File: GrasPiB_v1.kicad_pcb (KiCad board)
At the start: 2 copper layers, 85 x 56 mm, 45 parts, among them J1 DB9_Male, J2 Conn_GPIB, J3 JST_PH, J4 JST_PH, J5 3,5mm Pitch, J6 10pin IDC, U1 RPi_GPIO, U2 MAX3232, U3 SN75160BDW, U4 SN75161BDW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

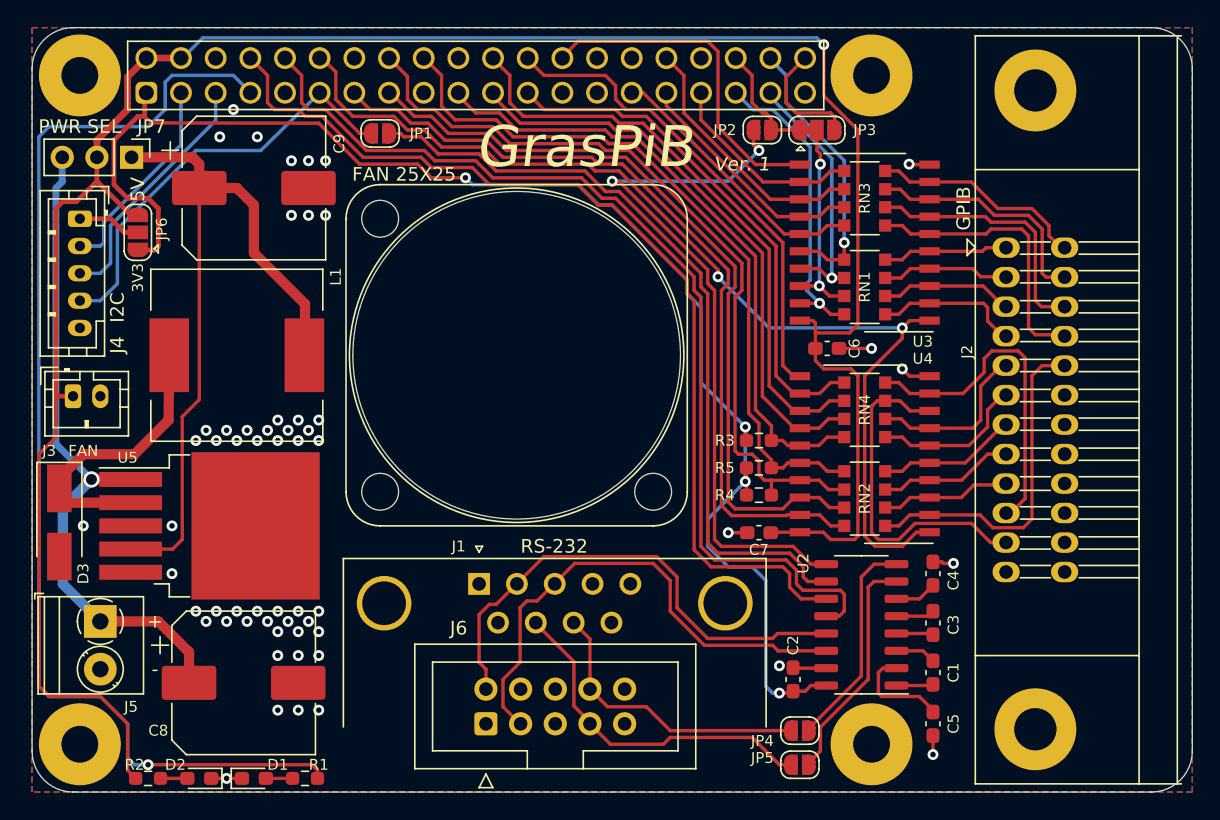
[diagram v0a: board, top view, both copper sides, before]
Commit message: Convert design files to KiCAD 6
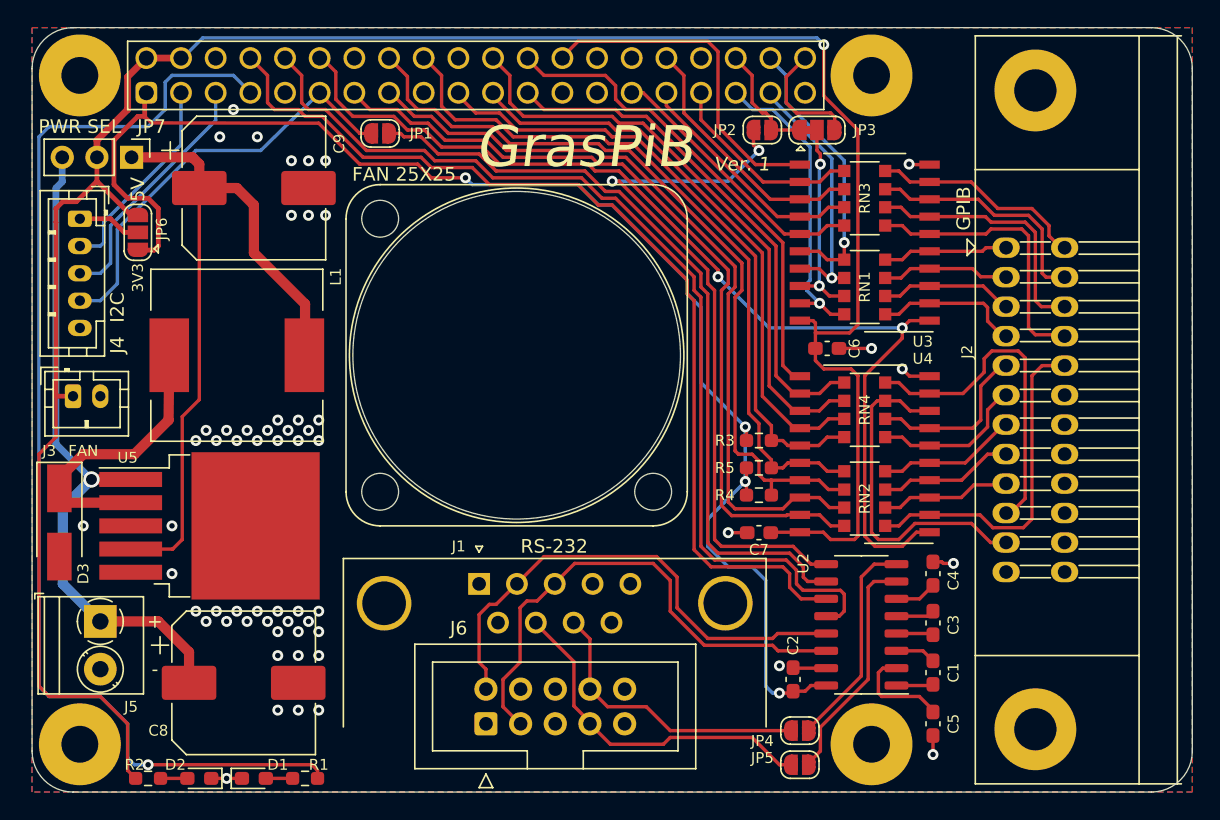
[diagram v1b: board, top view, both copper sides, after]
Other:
- net class Default removed
